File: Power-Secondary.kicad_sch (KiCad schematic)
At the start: 34 parts, among them J1 SUPP PWR MON, J2 SUPP PWR 1, J3 SUPP PWR 2, J4 DCDC SUPPLY, J5 FUSE +12V, Q1 S1G1D2S2G2D1, Q1A1 SUP90P06, Q1A2 SUP90P06, Q1A3 SUP90P06, Q1A4 SUP90P06, Q2 S1G1D2S2G2D1, Q3 S1G1D2S2G2D1

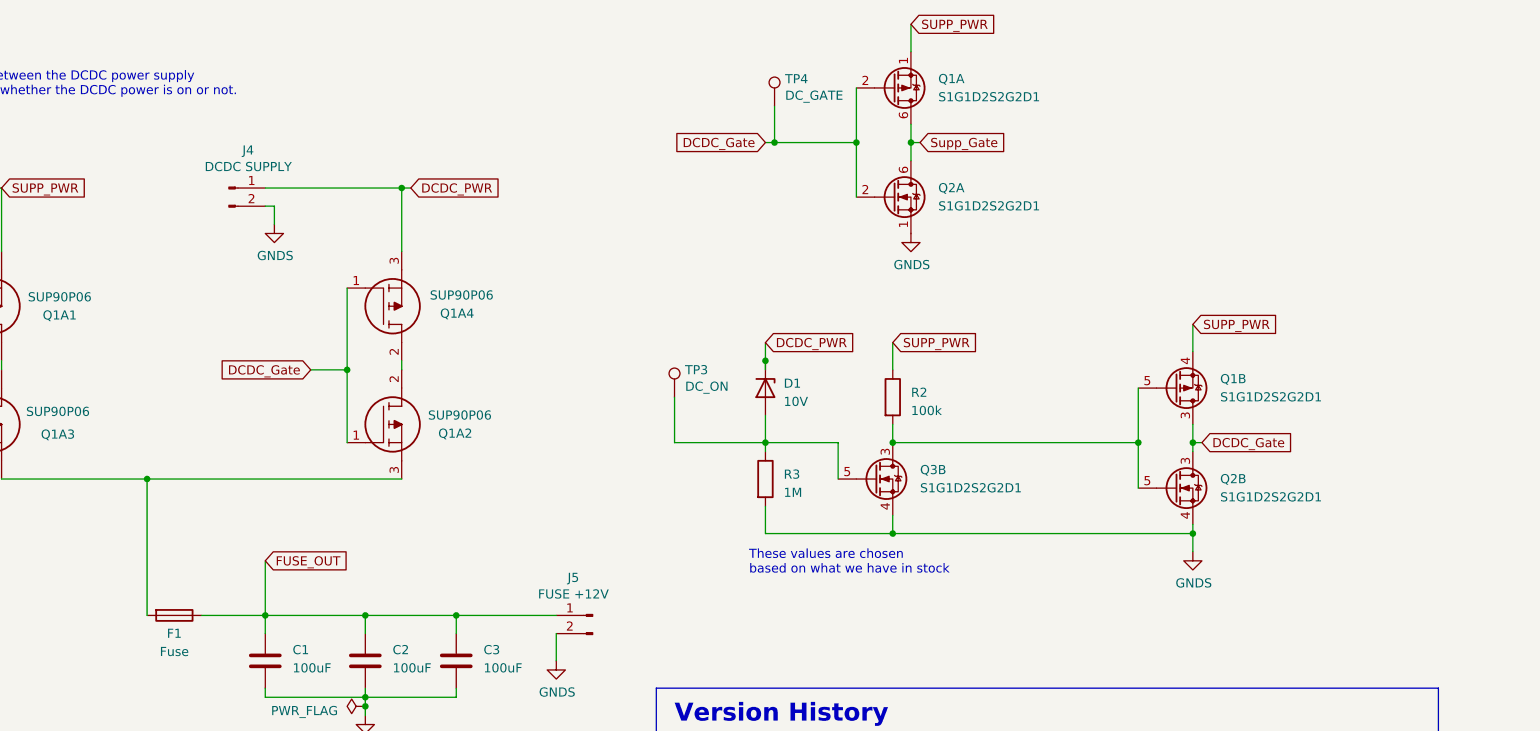
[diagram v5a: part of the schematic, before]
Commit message: Corrected gate labels
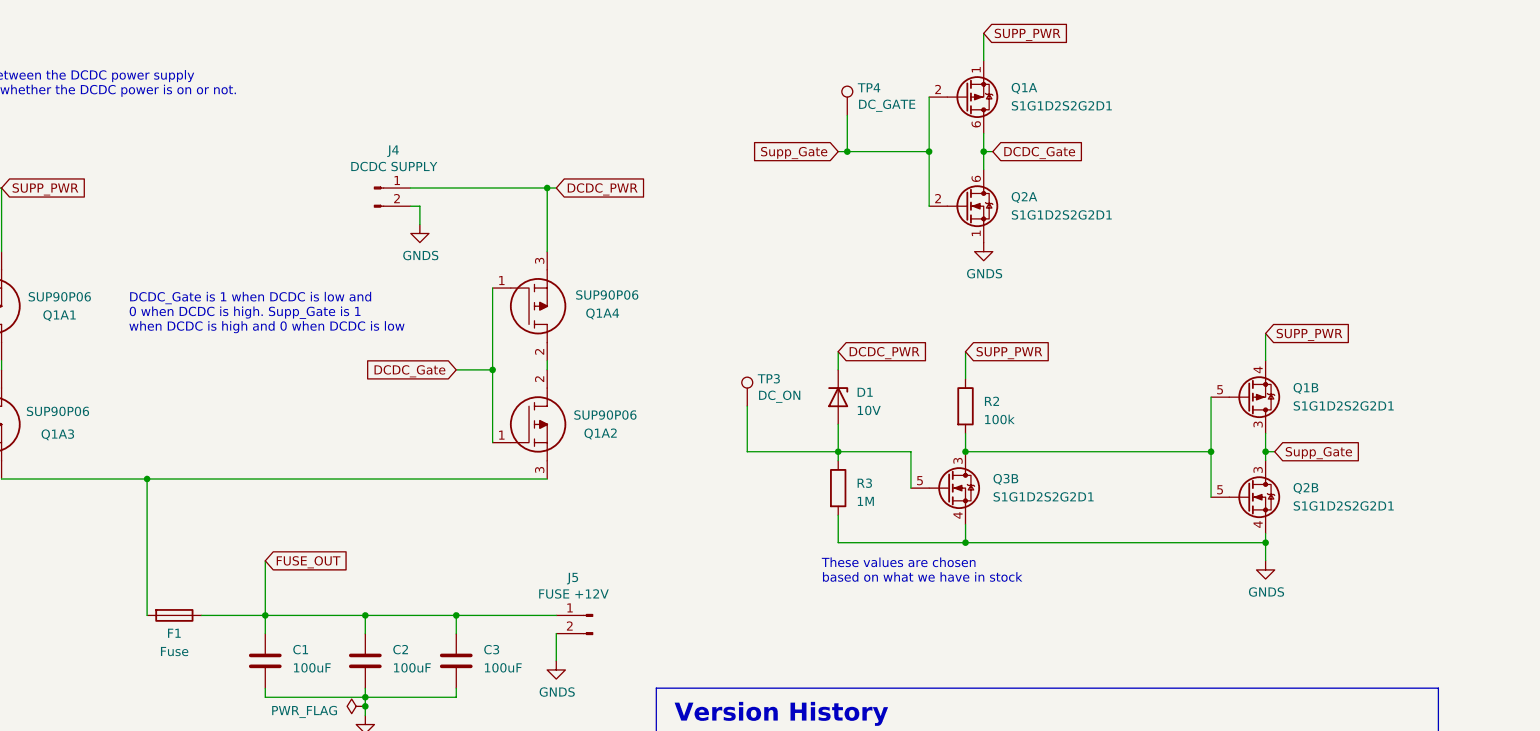
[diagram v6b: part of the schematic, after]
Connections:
- net DCDC_Gate: now also Q1.6 (D), Q2.6 (D); no longer Q1.2 (G), Q1.3 (D), Q2.2 (G), Q2.3 (D), TP4.1
- net Supp_Gate: now also Q1.2 (G), Q1.3 (D), Q2.2 (G), Q2.3 (D), TP4.1; no longer Q1.6 (D), Q2.6 (D)
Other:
- note added: "DCDC_Gate is 1 when DCDC is low and 0 when DCDC is high. Supp_Gate is 1 when DCDC is high and 0 when DCDC is low"
- moved on the sheet: D1, J4, Q1A, Q1A2, Q1A4, Q1B, Q2A, Q2B, Q3B, R2, R3, TP3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

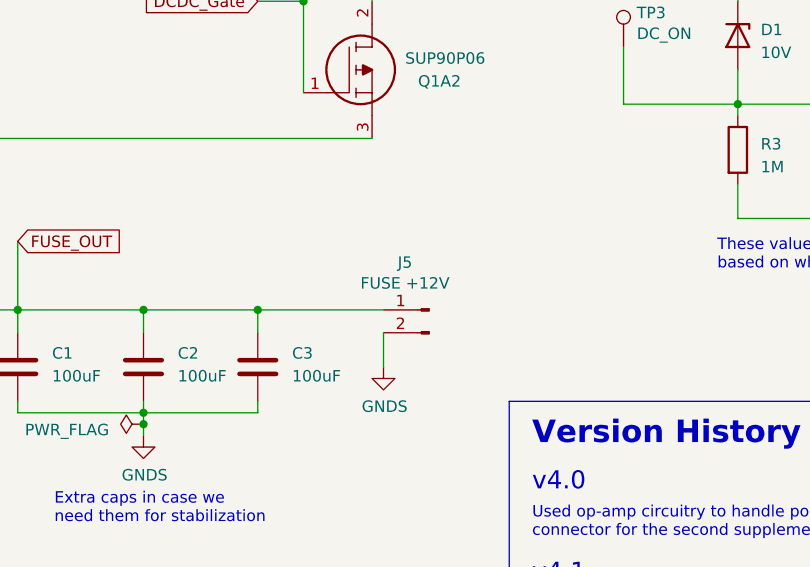
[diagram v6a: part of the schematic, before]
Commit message: Updated layout with zener diode
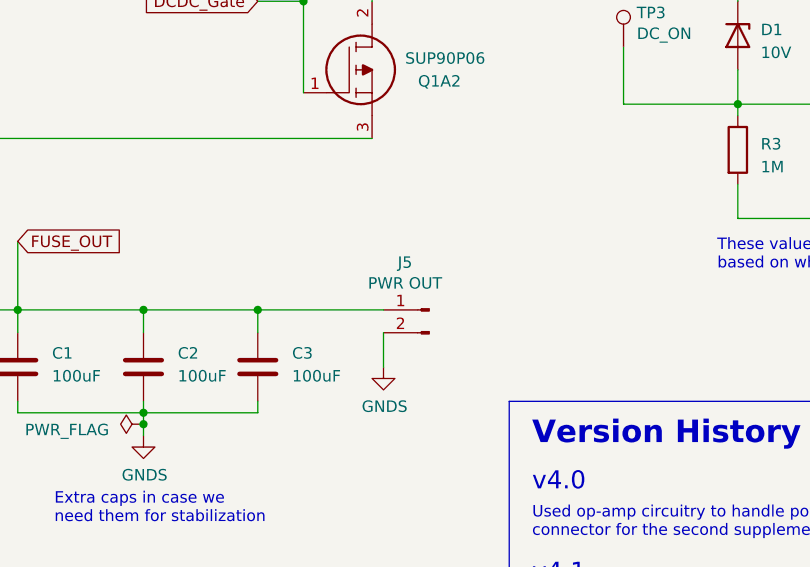
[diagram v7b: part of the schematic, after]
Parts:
- J5: value FUSE +12V -> PWR OUT
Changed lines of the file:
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@@
       (effects (font (size 1.27 1.27)) (justify bottom))
     )
-    (property "Value" "FUSE +12V" (at 142.0876 98.1202 0)
+    (property "Value" "PWR OUT" (at 142.0876 98.1202 0)
       (effects (font (size 1.27 1.27)) (justify bottom))
     )

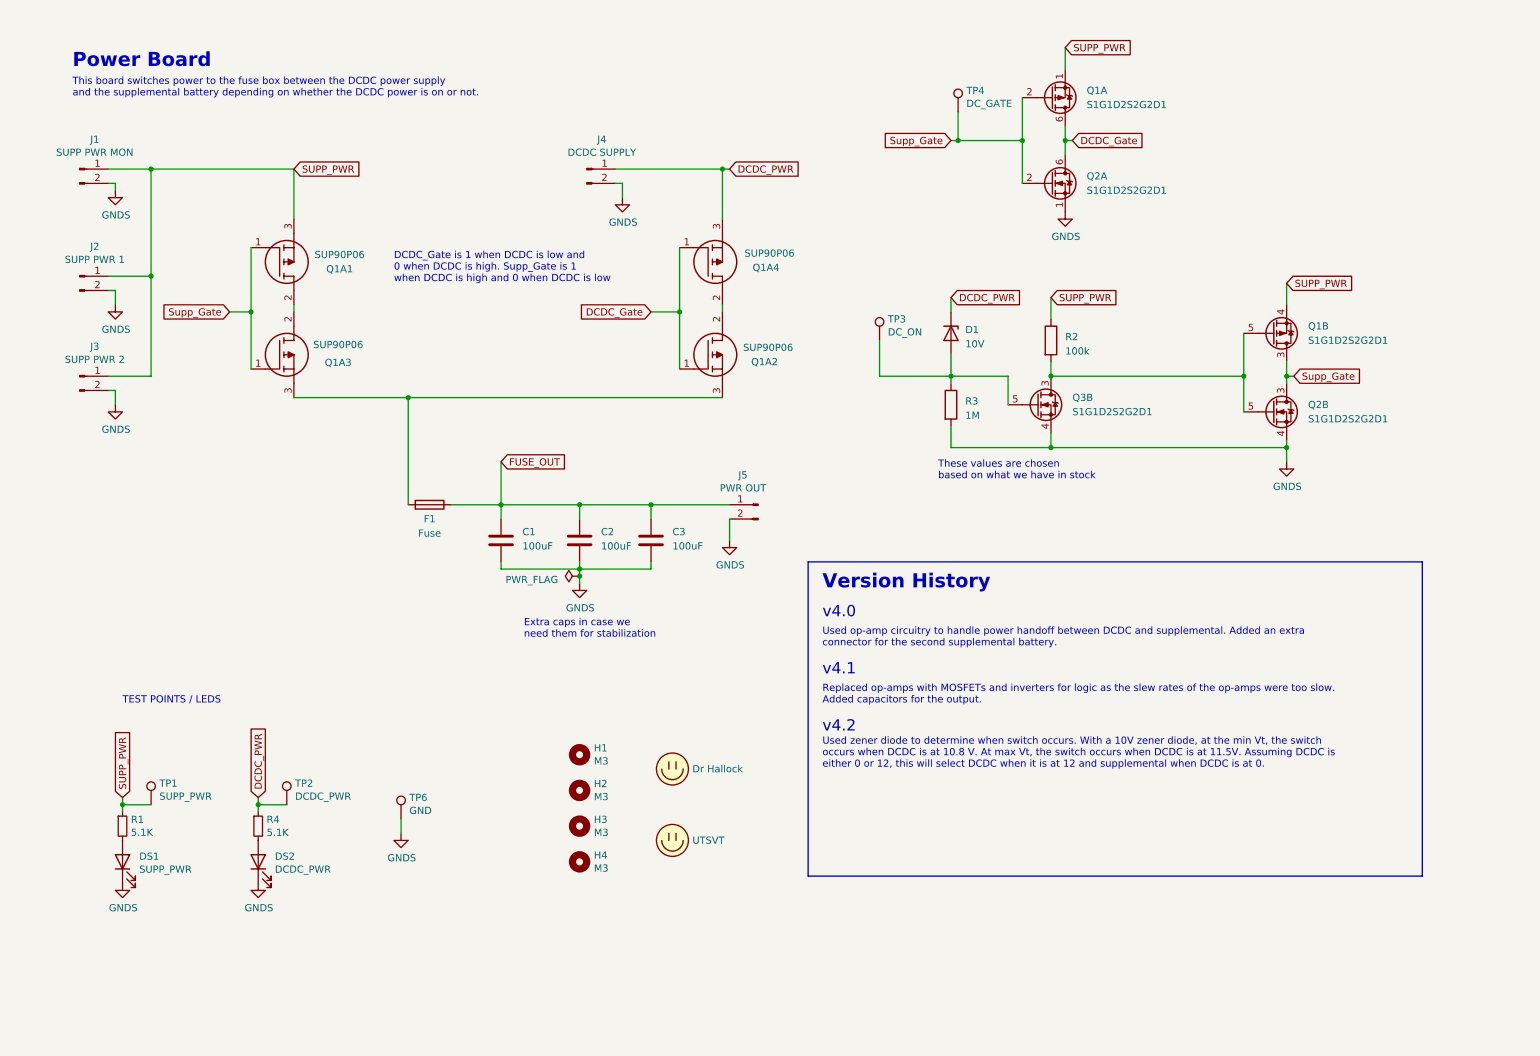
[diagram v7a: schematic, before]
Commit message: Updated schematic to interface with ignition switch
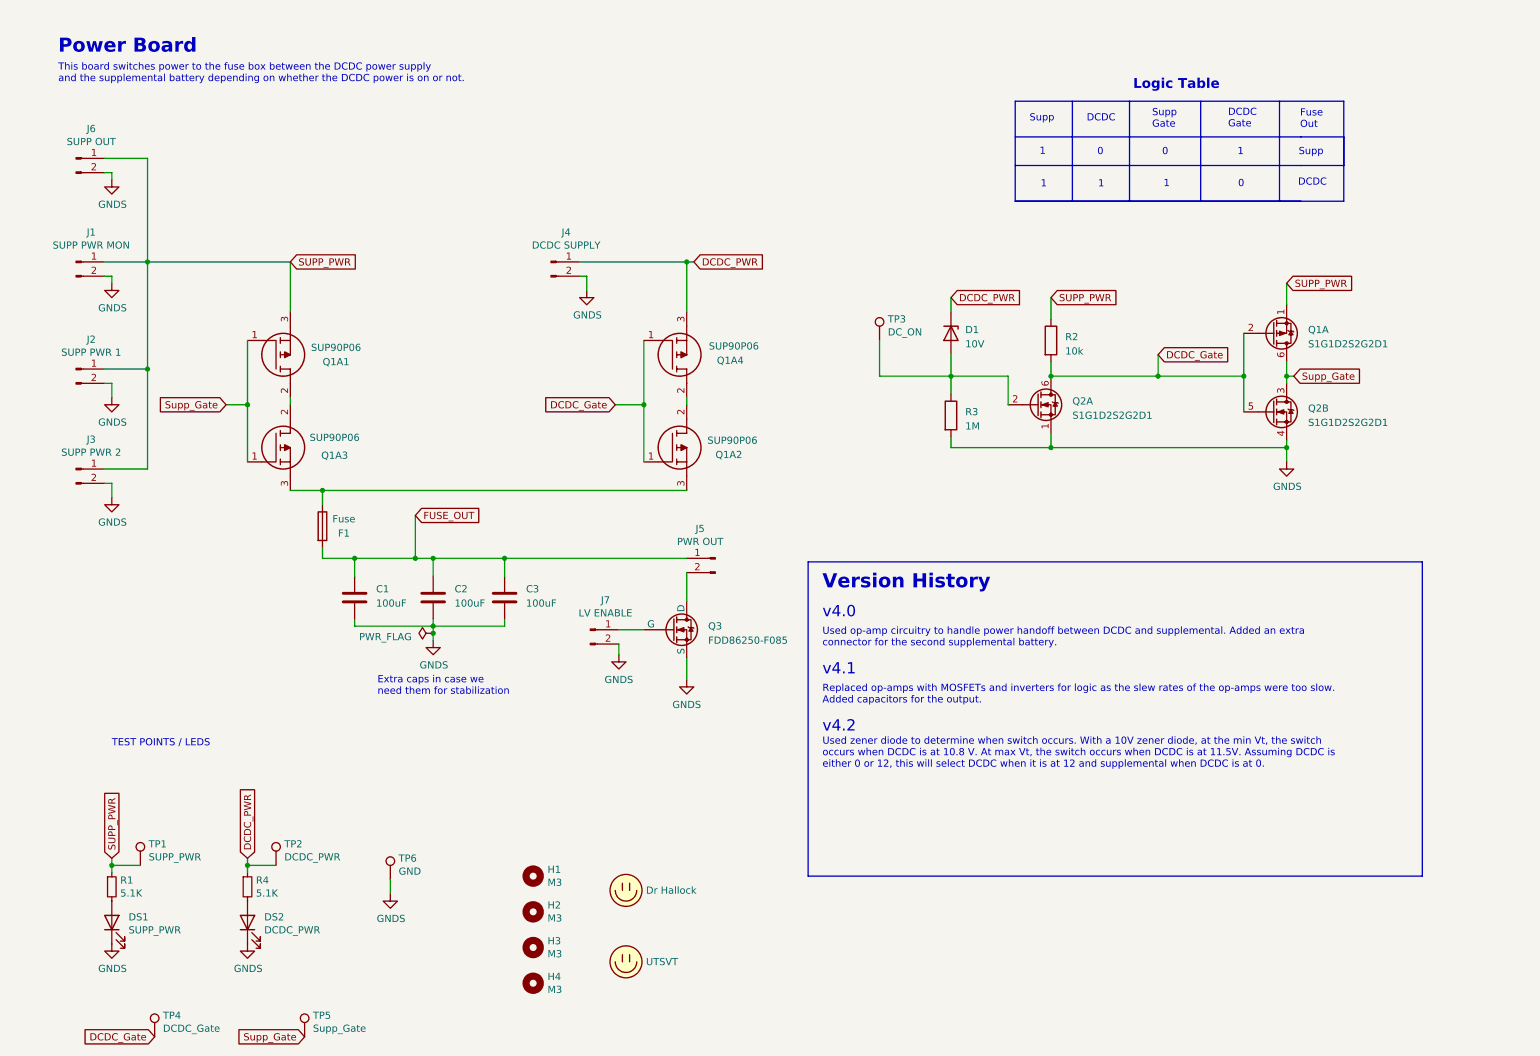
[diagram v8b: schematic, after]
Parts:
- removed unit 1 of Q1
- removed Q3: S1G1D2S2G2D1, UTSVT_PowerSupp:SOT65P210X100-6N, symbol Device:Q_Dual_NMOS_S1G1D2S2G2D1
- added J6: SUPP OUT, Connector_Molex:Molex_Micro-Fit_3.0_43650-0215_1x02_P3.00mm_Vertical, symbol Connector:Conn_01x02_Pin
- added J7: LV ENABLE, Connector_Molex:Molex_Micro-Fit_3.0_43650-0215_1x02_P3.00mm_Vertical, symbol Connector:Conn_01x02_Pin
- added Q3: FDD86250-F085, UTSVT_PowerSupp:FDD13AN06A0F085, symbol Simulation_SPICE:NMOS
- added TP5: Supp_Gate, TestPoint:TestPoint_Pad_2.0x2.0mm, symbol Connector:TestPoint
- R2: value 100k -> 10k
- TP4: value DC_GATE -> DCDC_Gate
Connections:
- net DCDC_Gate: now also Q1.2 (G), Q2.5 (G), R2.2, TP4.1
- net FUSE_OUT: now also F1.2; no longer F1.1
- net GNDS: now also J6.2 (Pin_2), J7.2 (Pin_2), Q3.3 (S); no longer J5.2 (Pin_2)
- net SUPP_PWR: now also Q1.1 (S), J6.1 (Pin_1); no longer Q1.4 (S)
- net Supp_Gate: now also Q1.6 (D), TP5.1; no longer Q1.3 (D), Q2.2 (G), TP4.1
- net at D1.2 (A), R3.1, TP3.1: now also Q2.2 (G)
- net at Q1A2.3, Q1A3.3: now also F1.1; no longer F1.2
- new net: J7.1 (Pin_1), Q3.1 (G)
- new net: J5.2 (Pin_2), Q3.2 (D)
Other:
- note added: "0"
- note added: "1"
- note added: "DCDC"
- note added: "DCDC Gate"
- note added: "Fuse Out"
- note added: "Logic Table"
- note added: "Supp"
- note added: "Supp Gate"
- note removed: "DCDC_Gate is 1 when DCDC is low and 0 when DCDC is high. Supp_Gate is 1 when DCDC is high and 0 when DCDC is low"
- note removed: "These values are chosen based on what we have in stock"
- moved on the sheet: C1, C2, C3, DS1, DS2, F1, H1, H2, H3, H4, J1, J2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
